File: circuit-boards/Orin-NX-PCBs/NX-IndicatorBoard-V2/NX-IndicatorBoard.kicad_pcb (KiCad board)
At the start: 4 copper layers, 100.4 x 79 mm, 52 parts, among them J1 NX Expansion, J2 CAN1, J3 CAN1, J4 CAN2, J5 CAN2, J6 PC LED, U1 74LVC245ABQ, U2 MCP2518FD-xQBB, U3 MCP2518FD-xQBB, U4 40MHz, U5 40MHz, U6 MCP2558FD, U7 MCP2558FD

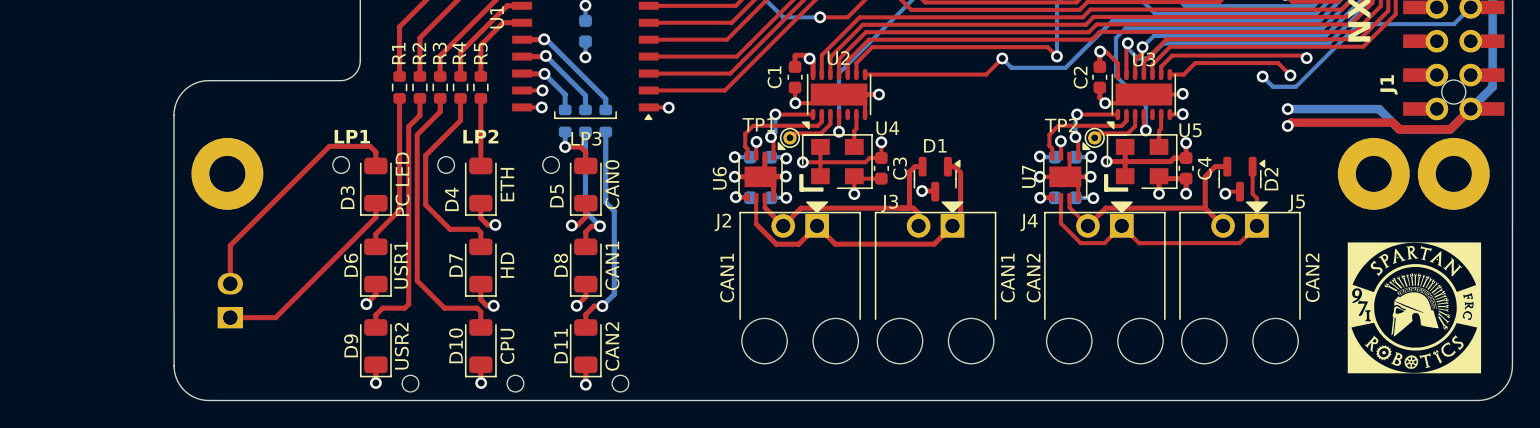
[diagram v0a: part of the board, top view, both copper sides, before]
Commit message: Moved LED connector to clear lower board
Signed-off-by: Scott <sgberman1@gmail.com>
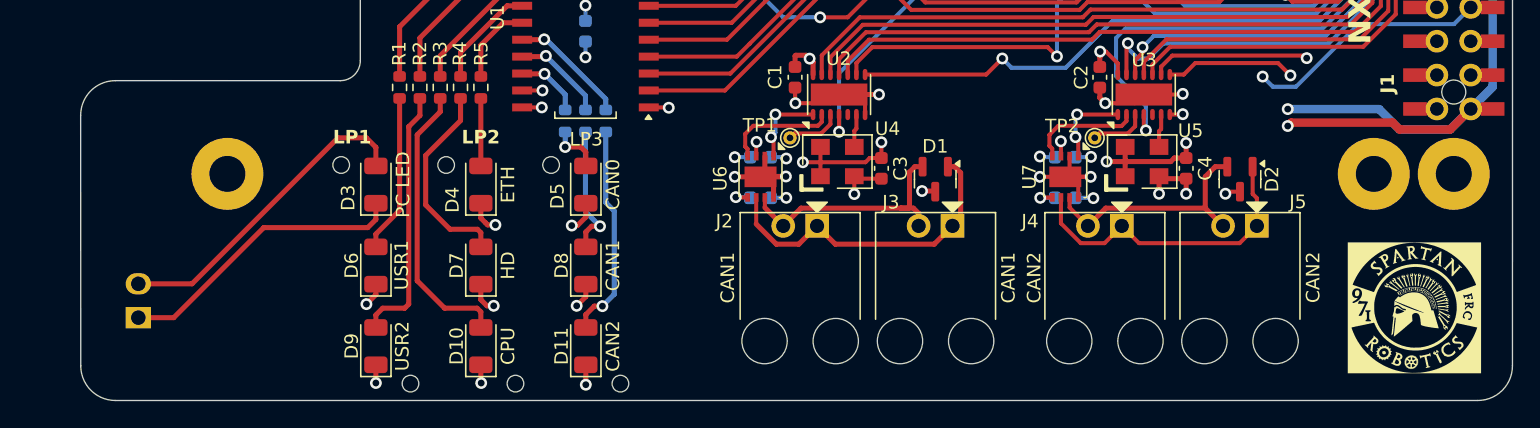
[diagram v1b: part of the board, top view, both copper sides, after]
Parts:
- moved J6 6.90 mm to (59.3, 119.8)
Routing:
- net /NX_PC_LED-: track 15.1 -> 22.1 mm
- net /NX_PC_LED+: track 18.1 -> 24.0 mm
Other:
- board size 100.4 x 79 mm -> 107.4 x 79 mm
- board text added: "0.0000 mm"
- board text added: "0.3048 mm / 0.2499 mm"
- board text added: "1.6000 mm"
- board text added: "107.4248 mm x 79.0000 mm"
- board text removed: "0.00 mils"
- board text removed: "12.00 mils / 9.84 mils"
- board text removed: "3953.73 mils x 3110.24 mils"
- board text removed: "62.99 mils"

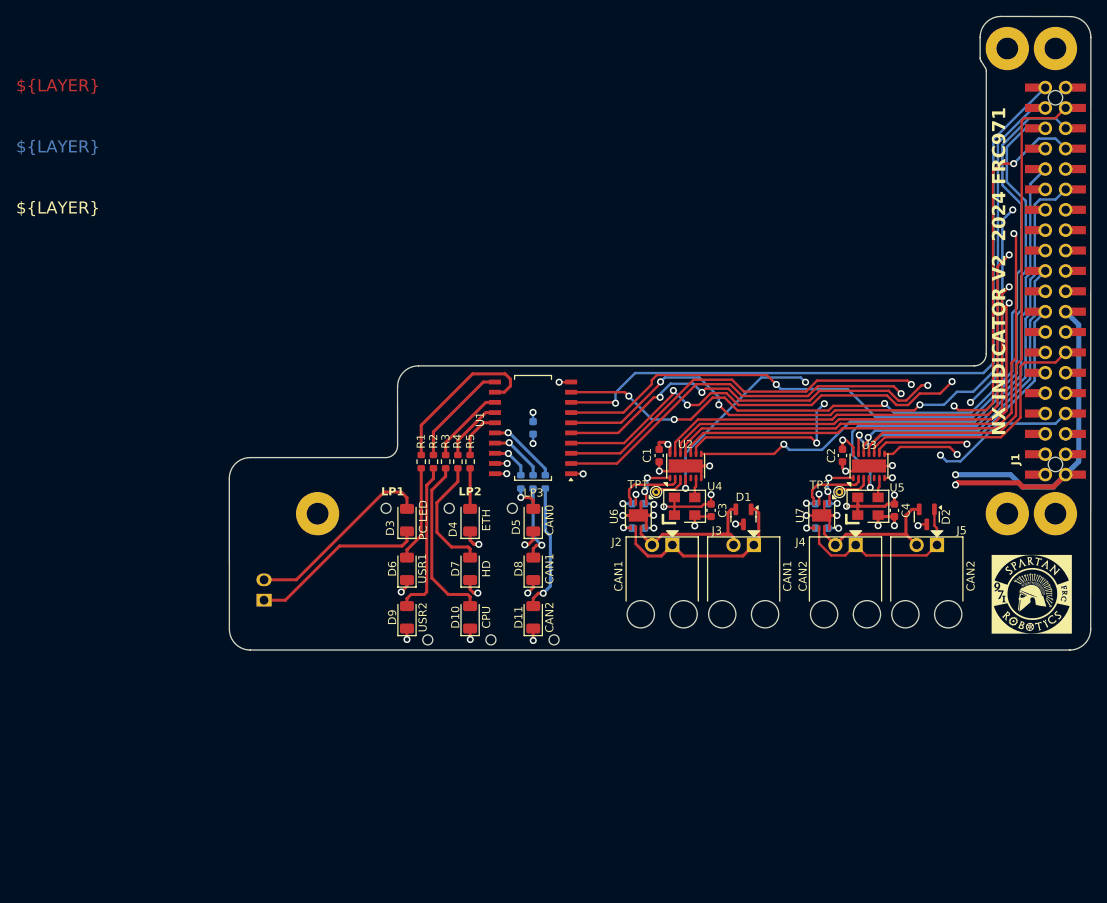
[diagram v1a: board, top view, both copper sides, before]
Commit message: Check in of NX Adapter and Indicator boards.  Complete pending review
Signed-off-by: Scott <sgberman1@gmail.com>
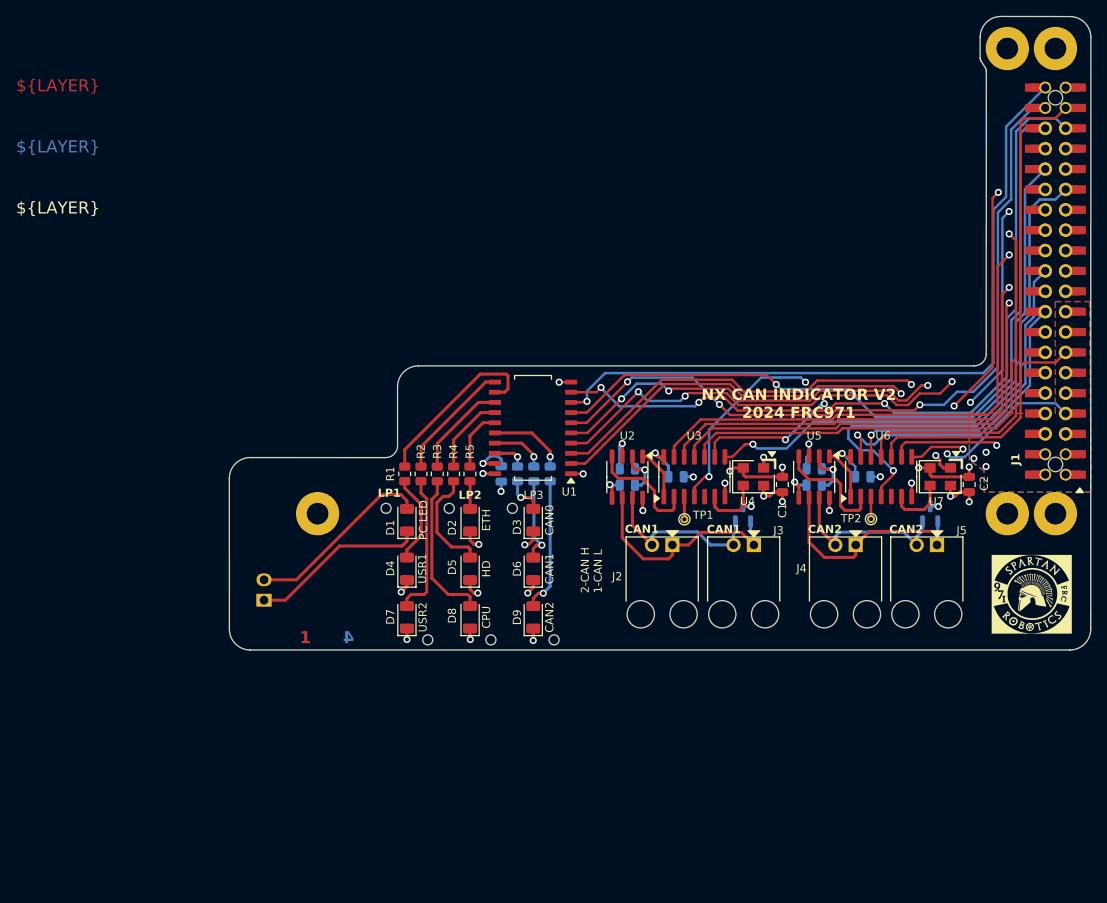
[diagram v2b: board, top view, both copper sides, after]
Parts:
- removed the U7 at (128.9, 109.2)
- added U5: MCP2558FD, Package_SO:SO-8_3.9x4.9mm_P1.27mm, F.Cu at (127.9, 104.4)
- C1, C2, C5, C6, C7, C8, C9: value 0.1uF-10%-50V-0603 -> 0.1uF-10%-50V-0805; footprint Capacitor_SMD:C_0603_1608Metric -> Capacitor_SMD:C_0805_2012Metric
- C3, C4: value 0.1uF-10%-50V-0603 -> 0.1uF-10%-50V-0805; footprint Capacitor_SMD:C_0603_1608Metric -> Capacitor_SMD:C_0805_2012Metric; moved to B.Cu
- D10: renamed from D2; moved to B.Cu
- D11: renamed from D1; moved to B.Cu
- R1, R2, R3, R4, R5, R6, R7, R8: value 499R-1%-0603 -> 499R-1%-0805; footprint Resistor_SMD:R_0603_1608Metric -> Resistor_SMD:R_0805_2012Metric
- U2: value MCP2518FD-xQBB -> MCP2558FD; footprint Package_DFN_QFN:DFN-14-1EP_3x4.5mm_P0.65mm_EP1.65x4.25mm -> Package_SO:SO-8_3.9x4.9mm_P1.27mm
- U3: value MCP2518FD-xQBB -> MCP2518FDT-H/SL; footprint Package_DFN_QFN:DFN-14-1EP_3x4.5mm_P0.65mm_EP1.65x4.25mm -> Package_SO:SO-14_3.9x8.65mm_P1.27mm
- U6: value MCP2558FD -> MCP2518FDT-H/SL; footprint Package_DFN_QFN:DFN-8-1EP_3x3mm_P0.65mm_EP1.55x2.4mm -> Package_SO:SO-14_3.9x8.65mm_P1.27mm
- moved C4 33.7 mm to (104.6, 103.4), turned to 0 degrees
- moved U6 30.7 mm to (136.3, 104.4), turned to 90 degrees
- moved U3 21.8 mm to (113.0, 104.4)
- moved C2 16.2 mm to (147.2, 105.4), turned to 90 degrees
- moved C1 15.8 mm to (124.0, 105.4), turned to 90 degrees
- moved C3 13.9 mm to (127.9, 103.4), turned to 0 degrees
- moved U7 9.74 mm to (143.6, 104.4), turned to 180 degrees
- moved U4 9.34 mm to (120.3, 104.4), turned to 180 degrees
- moved U2 7.40 mm to (104.6, 104.4), turned to -90 degrees
- moved C5 6.98 mm to (88.9, 104.0)
- moved C6 6.13 mm to (134.0, 104.4)
- moved C7 5.77 mm to (110.7, 104.4)
- moved C9 5.53 mm to (104.6, 105.4)
- moved C8 5.44 mm to (127.9, 105.4)
- moved TP2 5.19 mm to (135.0, 109.7)
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- renumbered D3 to D1, D4 to D2, D5 to D3, D6 to D4, D7 to D5, D8 to D6, D9 to D7, D10 to D8, D11 to D9, U5 to U7
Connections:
- C3 pad 1: +3V3 -> +5V
- C4 pad 1: +3V3 -> +5V
- C6 pad 1: +5V -> +3V3
- C7 pad 1: +5V -> +3V3
- TP1 pad 1: Net-(U2-CLKO/SOF) -> Net-(U3-CLKO/SOF)
- TP2 pad 1: Net-(U3-CLKO/SOF) -> Net-(U6-CLKO/SOF)
- U2 pad 2: /SPI-CAN-FD1/CANRX -> GND
- U2 pad 3: Net-(U2-CLKO/SOF) -> +5V
- U2 pad 4: /GPIO09 -> /SPI-CAN-FD1/CANRX
- U2 pad 5: unconnected-(U2-OSC2-Pad5) -> +3V3
- U2 pad 6: Net-(U2-OSC1) -> /CAN1_L
- U2 pad 7: GND -> /CAN1_H
- U2 pad 8: /GPIO07 -> GND
- U3 pad 1: /SPI-CAN-FD2/CANTX -> /SPI-CAN-FD1/CANTX
- U3 pad 10: /SPI1_SCK -> /SPI0_SCK
- U3 pad 11: /SPI1_MOSI -> /SPI0_MOSI
- U3 pad 12: /SPI1_MISO -> /SPI0_MISO
- U3 pad 13: /SPI1_CS0 -> /SPI0_CS0
- U3 pad 2: /SPI-CAN-FD2/CANRX -> /SPI-CAN-FD1/CANRX
- U3 pad 4: /GPIO01 -> /GPIO09
- U3 pad 8: /GPIO13 -> /GPIO07
- U3 pad 9: /GPIO11 -> /GPIO12
- U4 pad 3: Net-(U2-OSC1) -> Net-(U3-OSC1)
- U6 pad 1: /SPI-CAN-FD1/CANTX -> /SPI-CAN-FD2/CANTX
- U6 pad 2: GND -> /SPI-CAN-FD2/CANRX
- U6 pad 3: +5V -> Net-(U6-CLKO/SOF)
- U6 pad 4: /SPI-CAN-FD1/CANRX -> /GPIO01
- U6 pad 5: +3V3 -> unconnected-(U6-OSC2-Pad5)
- U6 pad 6: /CAN1_L -> Net-(U6-OSC1)
- U6 pad 7: /CAN1_H -> GND
- U6 pad 8: GND -> /GPIO13
- U6 pad 9: GND -> /GPIO11
- U7 pad 3: Net-(U3-OSC1) -> Net-(U6-OSC1)
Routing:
- net +3V3: track 83.9 -> 37.4 mm, vias 12 -> 15
- net +5V: track 4.51 -> 13.0 mm, vias 4 -> 2
- net /GPIO13: track 62.6 -> 54.1 mm
- net GND: track 71.7 -> 79.6 mm, vias 30 -> 25
- net Net-(U6-OSC1): track 0.00 -> 7.49 mm
- net /SPI-CAN-FD2/CANRX: track 8.40 -> 14.6 mm
- net /SPI-CAN-FD1/CANRX: track 8.41 -> 14.4 mm
- net Net-(U3-OSC1): track 2.49 -> 7.86 mm
- net /CAN2_L: track 23.4 -> 28.8 mm
- net /GPIO11: track 52.4 -> 57.6 mm
- net /GPIO01: track 60.2 -> 65.3 mm
- net Net-(U2-CLKO/SOF): track 4.18 -> 0.00 mm
- net /CAN1_L: track 24.4 -> 28.4 mm
- net /CAN2_H: track 18.3 -> 22.1 mm
- net /CAN1_H: track 19.0 -> 22.1 mm
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- added copper zone on B.Cu, net +3V3
- added copper zone on F.Cu, net +3V3
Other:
- board text added: "1. 4 layer PCB 2. PCB Thickness: 1.6 mm 3. Solder mask color: GREEN 4. Material: FR4-TG155 5. Surface Finish: HASL (with lead) 6. Outer Copper Weight: 1 oz 7. Inner Copper Weight: 0.5 oz 8. Impedance Control: NO 9. Via Covering: Plugged 10. Minimum Via Size/Hole Diameter: 0.89 mm/ 0.508 mm 11. Board Outline Tolerance: +/-0.2 mm"
- board text added: "2"
- board text added: "2-CAN H 1-CAN L"
- board text added: "2-LED+ 1-LED-"
- board text added: "3"
- board text added: "NOTES"
- board text added: "NX CAN INDICATOR V2 2024 FRC971"
- board text removed: "NX INDICATOR V2 2024 FRC971"

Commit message: Intermediate checkin of NX-Indicator-board
Signed-off-by: Scott Berman <scott.berman@bluerivertech.com>
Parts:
- removed D2: ETH, LED_SMD:LED_1206_3216Metric
- removed D4: USR1, LED_SMD:LED_1206_3216Metric
- removed D7: USR2, LED_SMD:LED_1206_3216Metric
- removed H1, H4: MountingHole, MountingHole:MountingHole_2.7mm_M2.5_Pad
- removed R1, R2, R5: 499R-1%-0805, Resistor_SMD:R_0805_2012Metric
- LP1, LP2, LP3: value Lumex-3x-Light-Pipe -> Lumex-2x-Light-Pipe; footprint NX-IndicatorBoard:LUMEX-LPF-C013301S -> NX-IndicatorBoard:Lumex-LPF-C012303S
- moved LP2 37.7 mm to (47.8, 110.9), turned to 0 degrees
- moved LP3 34.6 mm to (79.4, 148.4), turned to 0 degrees
- moved LP1 32.4 mm to (66.1, 147.0), turned to 0 degrees
- moved D5 31.3 mm to (85.6, 147.2)
- moved D6 31.3 mm to (93.5, 147.2)
- moved D3 31.3 mm to (93.5, 141.1)
- moved D8 31.3 mm to (85.6, 153.2)
- moved D9 31.3 mm to (93.5, 153.2)
- moved D1 30.9 mm to (84.6, 139.8)
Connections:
- U1 pad 11: Net-(U1-B7) -> unconnected-(U1-B7-Pad11)
- U1 pad 12: Net-(U1-B6) -> unconnected-(U1-B6-Pad12)
- U1 pad 15: Net-(U1-B3) -> unconnected-(U1-B3-Pad15)
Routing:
- net /NX_PC_LED+: track 23.6 -> 0.00 mm
- net Net-(U1-B6): track 22.4 -> 0.00 mm
- net /NX_PC_LED-: track 22.1 -> 0.00 mm
- net Net-(D8-A): track 19.3 -> 0.00 mm
- net Net-(D7-A): track 17.9 -> 0.00 mm
- net Net-(D9-A): track 16.8 -> 0.00 mm, vias 1 -> 0
- net GND: track 79.6 -> 64.6 mm, vias 25 -> 17
- net Net-(U1-B7): track 15.0 -> 0.00 mm
- net /UART1_CTS: track 97.1 -> 111.1 mm
- net Net-(D5-A): track 13.7 -> 0.00 mm
- net Net-(D4-A): track 11.1 -> 0.00 mm
- net Net-(D6-A): track 10.7 -> 0.00 mm, vias 1 -> 0
- net /GPIO13: track 54.1 -> 64.6 mm, vias 3 -> 2
- net Net-(U1-B3): track 7.62 -> 0.00 mm
- net /I2S0_FS: track 99.5 -> 106.2 mm, vias 3 -> 1
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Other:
- outline, holes or cut-outs redrawn
- copper layers 4 -> 6
